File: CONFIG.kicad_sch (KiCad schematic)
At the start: 24 parts, among them IC1 ECP5-BGA256, J1 Conn_ARM_JTAG_SWD_10, U5 AT25SF081-SSHD-X

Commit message: Change box around voltage labels
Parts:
- gave numbers to parts that had none: 7
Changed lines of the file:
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@@
   (symbol (lib_id "power:VCC") (at 92.71 140.97 0) (mirror y) (unit 1)
     (in_bom yes) (on_board yes)
-    (property "Reference" "#PWR?" (id 0) (at 92.71 144.78 0)
+    (property "Reference" "#PWR0148" (id 0) (at 92.71 144.78 0)
       (effects (font (size 1.27 1.27)) hide)
     )
@@
   (symbol (lib_id "power:GND") (at 92.71 176.53 0) (unit 1)
     (in_bom yes) (on_board yes)
-    (property "Reference" "#PWR?" (id 0) (at 92.71 182.88 0)
+    (property "Reference" "#PWR0149" (id 0) (at 92.71 182.88 0)
       (effects (font (size 1.27 1.27)) hide)
     )
@@
   (symbol (lib_id "Device:R") (at 96.52 140.97 270) (mirror x) (unit 1)
     (in_bom yes) (on_board yes)
-    (property "Reference" "R?" (id 0) (at 96.52 138.43 90))
+    (property "Reference" "R12" (id 0) (at 96.52 138.43 90))
     (property "Value" "R" (id 1) (at 96.52 140.97 90))
     (property "Footprint" "Resistor_SMD:R_0402_1005Metric" (id 2) (at 96.52 142.748 90)
@@
   (symbol (lib_id "Device:R") (at 96.52 146.685 270) (mirror x) (unit 1)
     (in_bom yes) (on_board yes)
-    (property "Reference" "R?" (id 0) (at 96.52 144.145 90))
+    (property "Reference" "R13" (id 0) (at 96.52 144.145 90))
     (property "Value" "R" (id 1) (at 96.52 146.685 90))
     (property "Footprint" "Resistor_SMD:R_0402_1005Metric" (id 2) (at 96.52 148.463 90)
@@
   (symbol (lib_id "Device:R") (at 96.52 152.4 270) (mirror x) (unit 1)
     (in_bom yes) (on_board yes)
-    (property "Reference" "R?" (id 0) (at 96.52 149.86 90))
+    (property "Reference" "R14" (id 0) (at 96.52 149.86 90))
     (property "Value" "R" (id 1) (at 96.52 152.4 90))
     (property "Footprint" "Resistor_SMD:R_0402_1005Metric" (id 2) (at 96.52 154.178 90)
@@
   (symbol (lib_id "Device:R") (at 96.52 158.115 270) (mirror x) (unit 1)
     (in_bom yes) (on_board yes)
-    (property "Reference" "R?" (id 0) (at 96.52 155.575 90))
+    (property "Reference" "R15" (id 0) (at 96.52 155.575 90))
     (property "Value" "R" (id 1) (at 96.52 158.115 90))
     (property "Footprint" "Resistor_SMD:R_0402_1005Metric" (id 2) (at 96.52 159.893 90)
@@
   (symbol (lib_id "Device:R") (at 96.52 163.83 270) (mirror x) (unit 1)
     (in_bom yes) (on_board yes)
-    (property "Reference" "R?" (id 0) (at 96.52 161.29 90))
+    (property "Reference" "R16" (id 0) (at 96.52 161.29 90))
     (property "Value" "R" (id 1) (at 96.52 163.83 90))
     (property "Footprint" "Resistor_SMD:R_0402_1005Metric" (id 2) (at 96.52 165.608 90)
@@
   (symbol (lib_id "Device:R") (at 96.52 169.545 270) (mirror x) (unit 1)
     (in_bom yes) (on_board yes)
-    (property "Reference" "R?" (id 0) (at 96.52 167.005 90))
+    (property "Reference" "R17" (id 0) (at 96.52 167.005 90))
     (property "Value" "R" (id 1) (at 96.52 169.545 90))
     (property "Footprint" "Resistor_SMD:R_0402_1005Metric" (id 2) (at 96.52 171.323 90)
@@
   (symbol (lib_id "Device:R") (at 96.52 175.26 90) (mirror x) (unit 1)
     (in_bom yes) (on_board yes)
-    (property "Reference" "R?" (id 0) (at 96.52 172.5738 90))
+    (property "Reference" "R18" (id 0) (at 96.52 172.5738 90))
     (property "Value" "R" (id 1) (at 96.52 175.26 90))
     (property "Footprint" "Resistor_SMD:R_0402_1005Metric" (id 2) (at 96.52 173.482 90)

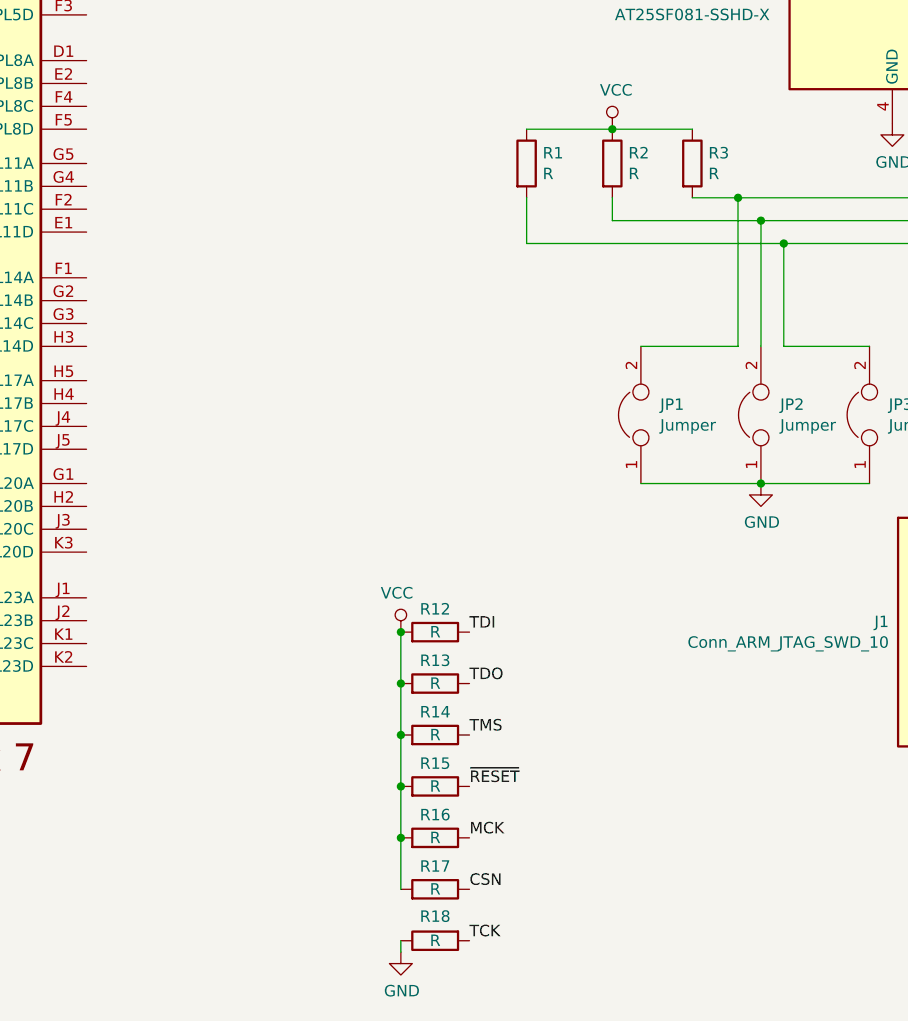
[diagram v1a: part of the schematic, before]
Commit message: Add semi-critical resistor values
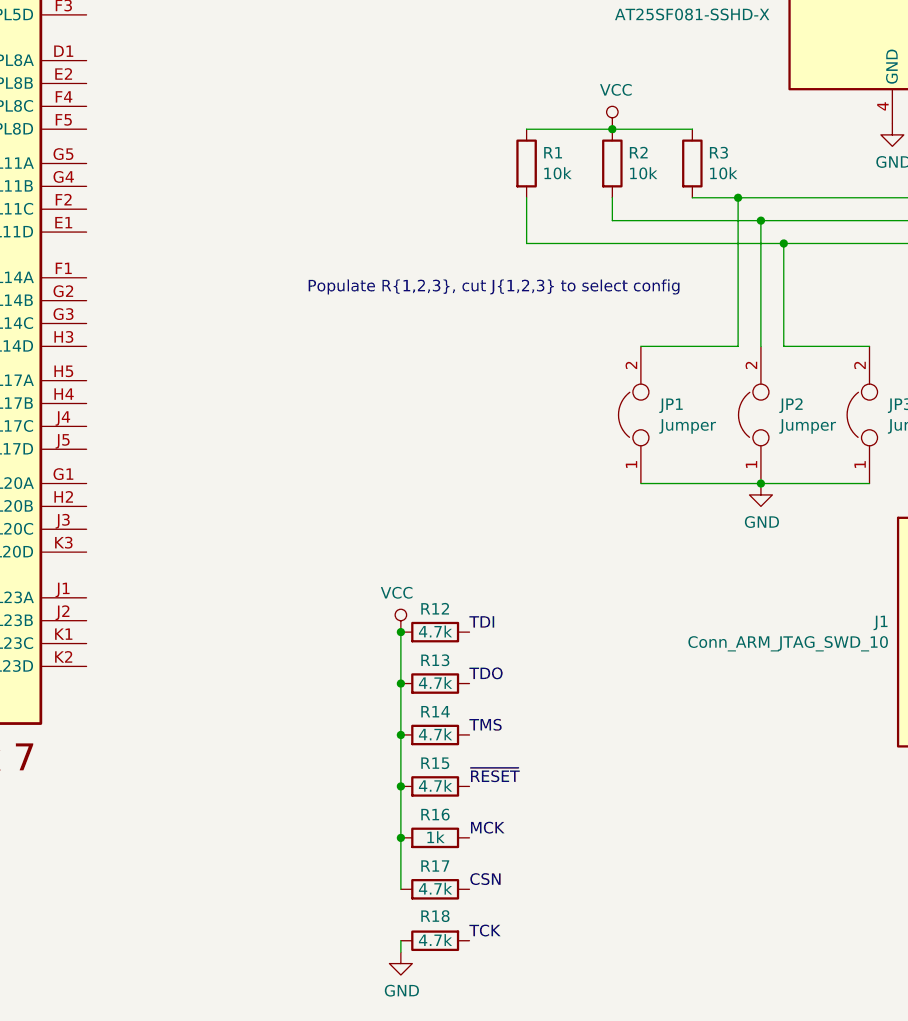
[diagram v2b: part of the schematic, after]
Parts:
- R1, R2, R3: value R -> 10k
- R12, R13, R14, R15, R17, R18: value R -> 4.7k
- R16: value R -> 1k
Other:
- note added: "Populate R{1,2,3}, cut J{1,2,3} to select config"
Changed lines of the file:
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@@
-(kicad_sch (version 20200618) (host eeschema "5.99.0-unknown-7340c97~102~ubuntu20.04.1")
+(kicad_sch (version 20200618) (host eeschema "5.99.0-unknown-e9da02e~102~ubuntu20.04.1")
   (page 4 6)
   (paper "A4")
@@
     (stroke (width 0) (type solid) (color 0 0 0 0))
   )
+  (text "Populate R{1,2,3}, cut J{1,2,3} to select config" (at 123.825 103.505 180)
+    (effects (font (size 1.27 1.27)) (justify right bottom))
+  )
   (label "TDI" (at 100.33 140.97 0)
     (effects (font (size 1.27 1.27)) (justify left bottom))
@@
     (in_bom yes) (on_board yes)
     (property "Reference" "R12" (id 0) (at 96.52 138.43 90))
-    (property "Value" "R" (id 1) (at 96.52 140.97 90))
+    (property "Value" "4.7k" (id 1) (at 96.52 140.97 90))
     (property "Footprint" "Resistor_SMD:R_0402_1005Metric" (id 2) (at 96.52 142.748 90)
       (effects (font (size 1.27 1.27)) hide)
@@
     (in_bom yes) (on_board yes)
     (property "Reference" "R13" (id 0) (at 96.52 144.145 90))
-    (property "Value" "R" (id 1) (at 96.52 146.685 90))
+    (property "Value" "4.7k" (id 1) (at 96.52 146.685 90))
     (property "Footprint" "Resistor_SMD:R_0402_1005Metric" (id 2) (at 96.52 148.463 90)
       (effects (font (size 1.27 1.27)) hide)
@@
     (in_bom yes) (on_board yes)
     (property "Reference" "R14" (id 0) (at 96.52 149.86 90))
-    (property "Value" "R" (id 1) (at 96.52 152.4 90))
+    (property "Value" "4.7k" (id 1) (at 96.52 152.4 90))
     (property "Footprint" "Resistor_SMD:R_0402_1005Metric" (id 2) (at 96.52 154.178 90)
       (effects (font (size 1.27 1.27)) hide)
@@
     (in_bom yes) (on_board yes)
     (property "Reference" "R15" (id 0) (at 96.52 155.575 90))
-    (property "Value" "R" (id 1) (at 96.52 158.115 90))
+    (property "Value" "4.7k" (id 1) (at 96.52 158.115 90))
     (property "Footprint" "Resistor_SMD:R_0402_1005Metric" (id 2) (at 96.52 159.893 90)
       (effects (font (size 1.27 1.27)) hide)
@@
     (in_bom yes) (on_board yes)
     (property "Reference" "R16" (id 0) (at 96.52 161.29 90))
-    (property "Value" "R" (id 1) (at 96.52 163.83 90))
+    (property "Value" "1k" (id 1) (at 96.52 163.83 90))
     (property "Footprint" "Resistor_SMD:R_0402_1005Metric" (id 2) (at 96.52 165.608 90)
       (effects (font (size 1.27 1.27)) hide)
@@
     (in_bom yes) (on_board yes)
     (property "Reference" "R17" (id 0) (at 96.52 167.005 90))
-    (property "Value" "R" (id 1) (at 96.52 169.545 90))
+    (property "Value" "4.7k" (id 1) (at 96.52 169.545 90))
     (property "Footprint" "Resistor_SMD:R_0402_1005Metric" (id 2) (at 96.52 171.323 90)
       (effects (font (size 1.27 1.27)) hide)
@@
     (in_bom yes) (on_board yes)
     (property "Reference" "R18" (id 0) (at 96.52 172.5738 90))
-    (property "Value" "R" (id 1) (at 96.52 175.26 90))
+    (property "Value" "4.7k" (id 1) (at 96.52 175.26 90))
     (property "Footprint" "Resistor_SMD:R_0402_1005Metric" (id 2) (at 96.52 173.482 90)
       (effects (font (size 1.27 1.27)) hide)
@@
       (effects (font (size 1.27 1.27)) (justify left))
     )
-    (property "Value" "R" (id 1) (at 108.4581 90.0493 0)
+    (property "Value" "10k" (id 1) (at 108.458 90.049 0)
       (effects (font (size 1.27 1.27)) (justify left))
     )
@@
       (effects (font (size 1.27 1.27)) (justify left))
     )
-    (property "Value" "R" (id 1) (at 117.9831 90.0493 0)
+    (property "Value" "10k" (id 1) (at 117.983 90.049 0)
       (effects (font (size 1.27 1.27)) (justify left))
     )
@@
       (effects (font (size 1.27 1.27)) (justify left))
     )
-    (property "Value" "R" (id 1) (at 126.8731 90.0493 0)
-      (effects (font (size 1.27 1.27)) (justify left))
-    )
+    (property "Value" "10k" (id 1) (at 126.873 90.049 0)
+      (effects (font (size 1.27 1.27)) (justify left))
+    )

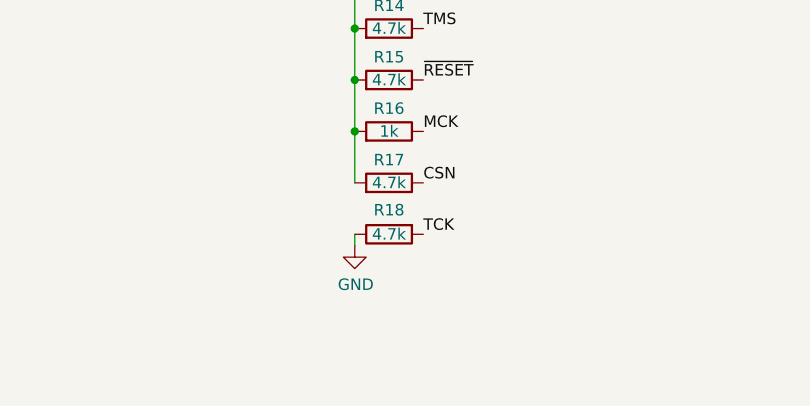
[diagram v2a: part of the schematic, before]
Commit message: Add more pullup resistors
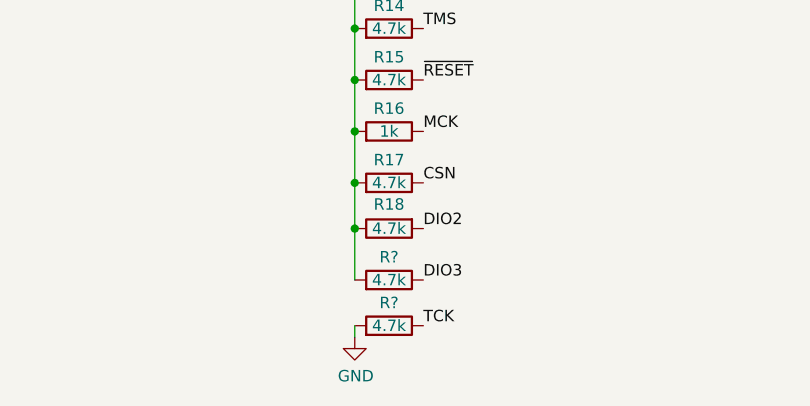
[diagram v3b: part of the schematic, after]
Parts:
- added R? (x2): 4.7k, Resistor_SMD:R_0402_1005Metric, symbol Device:R
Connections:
- net DIO2: now also R18.2
- net DIO3: now also R?.1
- net GND: now also R?.2; no longer R18.1
- net TCK: now also R?.1; no longer R18.2
- net VCC: now also R18.1, R?.2
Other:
- moved on the sheet: R18
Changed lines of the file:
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@@
-(kicad_sch (version 20200618) (host eeschema "5.99.0-unknown-e9da02e~102~ubuntu20.04.1")
+(kicad_sch (version 20200714) (host eeschema "5.99.0-unknown-9f20c61~102~ubuntu20.04.1")
   (page 4 6)
   (paper "A4")
@@
   (junction (at 92.71 158.115) (diameter 0) (color 0 0 0 0))
   (junction (at 92.71 163.83) (diameter 0) (color 0 0 0 0))
+  (junction (at 92.71 169.545) (diameter 0) (color 0 0 0 0))
+  (junction (at 92.71 174.625) (diameter 0) (color 0 0 0 0))
   (junction (at 116.205 85.09) (diameter 0) (color 0 0 0 0))
   (junction (at 130.175 92.71) (diameter 0) (color 0 0 0 0))
@@
     (stroke (width 0) (type solid) (color 0 0 0 0))
   )
-  (wire (pts (xy 92.71 175.26) (xy 92.71 176.53))
+  (wire (pts (xy 92.71 169.545) (xy 92.71 174.625))
+    (stroke (width 0) (type solid) (color 0 0 0 0))
+  )
+  (wire (pts (xy 92.71 174.625) (xy 92.71 180.34))
+    (stroke (width 0) (type solid) (color 0 0 0 0))
+  )
+  (wire (pts (xy 92.71 185.42) (xy 92.71 186.69))
     (stroke (width 0) (type solid) (color 0 0 0 0))
   )
@@
     (effects (font (size 1.27 1.27)) (justify left bottom))
   )
-  (label "TCK" (at 100.33 175.26 0)
+  (label "DIO2" (at 100.33 174.625 0)
+    (effects (font (size 1.27 1.27)) (justify left bottom))
+  )
+  (label "DIO3" (at 100.33 180.34 0)
+    (effects (font (size 1.27 1.27)) (justify left bottom))
+  )
+  (label "TCK" (at 100.33 185.42 0)
     (effects (font (size 1.27 1.27)) (justify left bottom))
   )
@@
     )
   )
-  (symbol (lib_id "power:GND") (at 92.71 176.53 0) (unit 1)
-    (in_bom yes) (on_board yes)
-    (property "Reference" "#PWR0149" (id 0) (at 92.71 182.88 0)
-      (effects (font (size 1.27 1.27)) hide)
-    )
-    (property "Value" "GND" (id 1) (at 92.8243 180.8544 0))
-    (property "Footprint" "" (id 2) (at 92.71 176.53 0)
-      (effects (font (size 1.27 1.27)) hide)
-    )
-    (property "Datasheet" "" (id 3) (at 92.71 176.53 0)
+  (symbol (lib_id "power:GND") (at 92.71 186.69 0) (unit 1)
+    (in_bom yes) (on_board yes)
+    (property "Reference" "#PWR0149" (id 0) (at 92.71 193.04 0)
+      (effects (font (size 1.27 1.27)) hide)
+    )
+    (property "Value" "GND" (id 1) (at 92.8243 191.0144 0))
+    (property "Footprint" "" (id 2) (at 92.71 186.69 0)
+      (effects (font (size 1.27 1.27)) hide)
+    )
+    (property "Datasheet" "" (id 3) (at 92.71 186.69 0)
       (effects (font (size 1.27 1.27)) hide)
     )
@@
     )
   )
-  (symbol (lib_id "Device:R") (at 96.52 175.26 90) (mirror x) (unit 1)
-    (in_bom yes) (on_board yes)
-    (property "Reference" "R18" (id 0) (at 96.52 172.5738 90))
-    (property "Value" "4.7k" (id 1) (at 96.52 175.26 90))
-    (property "Footprint" "Resistor_SMD:R_0402_1005Metric" (id 2) (at 96.52 173.482 90)
-      (effects (font (size 1.27 1.27)) hide)
-    )
-    (property "Datasheet" "~" (id 3) (at 96.52 175.26 0)
-      (effects (font (size 1.27 1.27)) hide)
-    )
+  (symbol (lib_id "Device:R") (at 96.52 174.625 90) (mirror x) (unit 1)
+    (in_bom yes) (on_board yes)
+    (property "Reference" "R18" (id 0) (at 96.52 171.9388 90))
+    (property "Value" "4.7k" (id 1) (at 96.52 174.625 90))
+    (property "Footprint" "Resistor_SMD:R_0402_1005Metric" (id 2) (at 96.52 172.847 90)
+      (effects (font (size 1.27 1.27)) hide)
+    )
+    (property "Datasheet" "~" (id 3) (at 96.52 174.625 0)
+      (effects (font (size 1.27 1.27)) hide)
+    )
+  )
+  (symbol (lib_id "Device:R") (at 96.52 180.34 270) (mirror x) (unit 1)
+    (in_bom yes) (on_board yes)
+    (property "Reference" "R?" (id 0) (at 96.52 177.8 90))
+    (property "Value" "4.7k" (id 1) (at 96.52 180.34 90))
+    (property "Footprint" "Resistor_SMD:R_0402_1005Metric" (id 2) (at 96.52 182.118 90)
+      (effects (font (size 1.27 1.27)) hide)
+    )
+    (property "Datasheet" "~" (id 3) (at 96.52 180.34 0)
+      (effects (font (size 1.27 1.27)) hide)
+    )
+  )
+  (symbol (lib_id "Device:R") (at 96.52 185.42 270) (mirror x) (unit 1)
+    (in_bom yes) (on_board yes)
+    (property "Reference" "R?" (id 0) (at 96.52 182.88 90))
+    (property "Value" "4.7k" (id 1) (at 96.52 185.42 90))
+    (property "Footprint" "Resistor_SMD:R_0402_1005Metric" (id 2) (at 96.52 187.198 90)
+      (effects (font (size 1.27 1.27)) hide)
+    )
+    (property "Datasheet" "~" (id 3) (at 96.52 185.42 0)
+      (effects (font (size 1.27 1.27)) hide)
+    )

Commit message: Remember to save the schematic
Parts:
- gave numbers to parts that had none: 2
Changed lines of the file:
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@@
   (symbol (lib_id "Device:R") (at 96.52 180.34 270) (mirror x) (unit 1)
     (in_bom yes) (on_board yes)
-    (property "Reference" "R?" (id 0) (at 96.52 177.8 90))
+    (property "Reference" "R19" (id 0) (at 96.52 177.8 90))
     (property "Value" "4.7k" (id 1) (at 96.52 180.34 90))
     (property "Footprint" "Resistor_SMD:R_0402_1005Metric" (id 2) (at 96.52 182.118 90)
@@
   (symbol (lib_id "Device:R") (at 96.52 185.42 270) (mirror x) (unit 1)
     (in_bom yes) (on_board yes)
-    (property "Reference" "R?" (id 0) (at 96.52 182.88 90))
+    (property "Reference" "R20" (id 0) (at 96.52 182.88 90))
     (property "Value" "4.7k" (id 1) (at 96.52 185.42 90))
     (property "Footprint" "Resistor_SMD:R_0402_1005Metric" (id 2) (at 96.52 187.198 90)
